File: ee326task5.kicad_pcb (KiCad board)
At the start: 2 copper layers, 41 parts, among them J1 694106106102, J2 Conn_01x03, J3 Conn_01x03, J4 Conn_01x03, J5 Conn_01x03, J6 2-1734592-4, SW1 MCU_RESET, SW2 PROVISIONING, SW3 WIFI_RESET, SW4 IO0, U1 ATSAM4S8BA-AU, U2 LDL1117S30R, U3 ESP32-WROOM-32, Y1 ABM7-12.000MHZ-D2Y-T

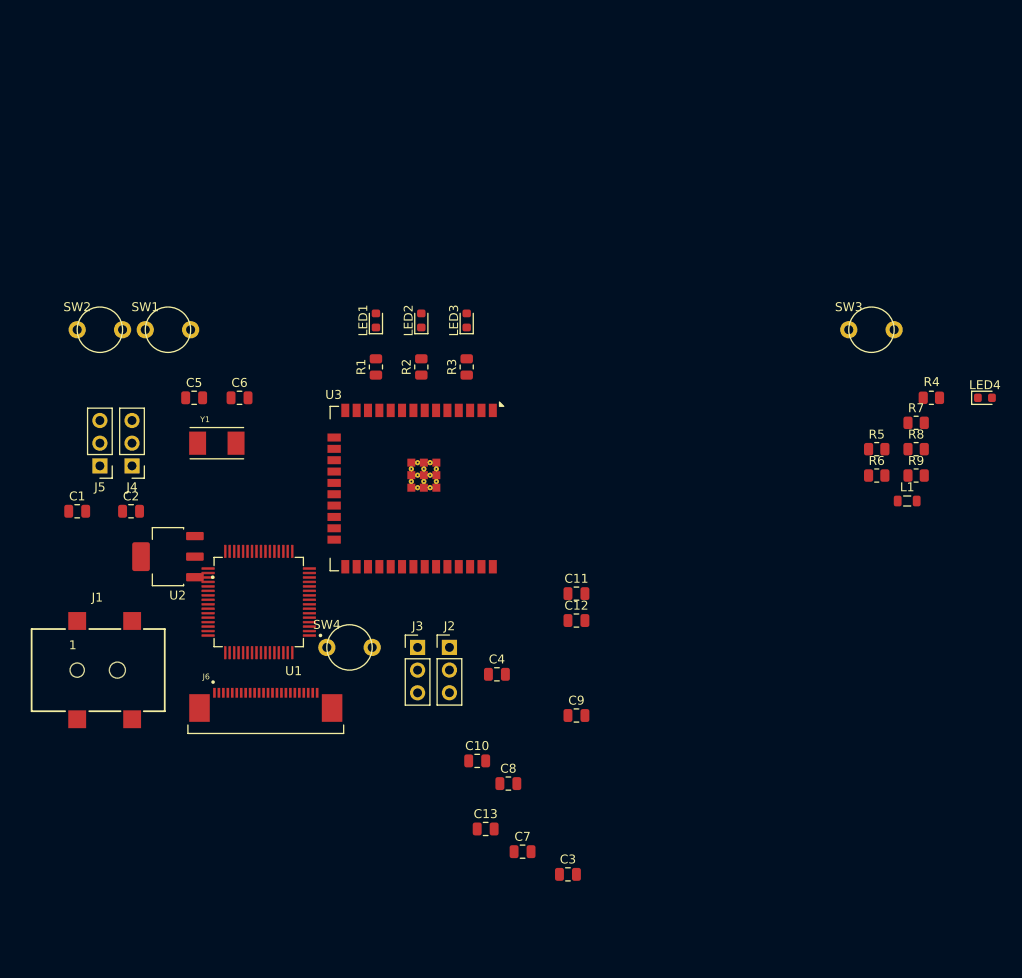
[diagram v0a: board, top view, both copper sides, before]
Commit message: fixed schematic errors
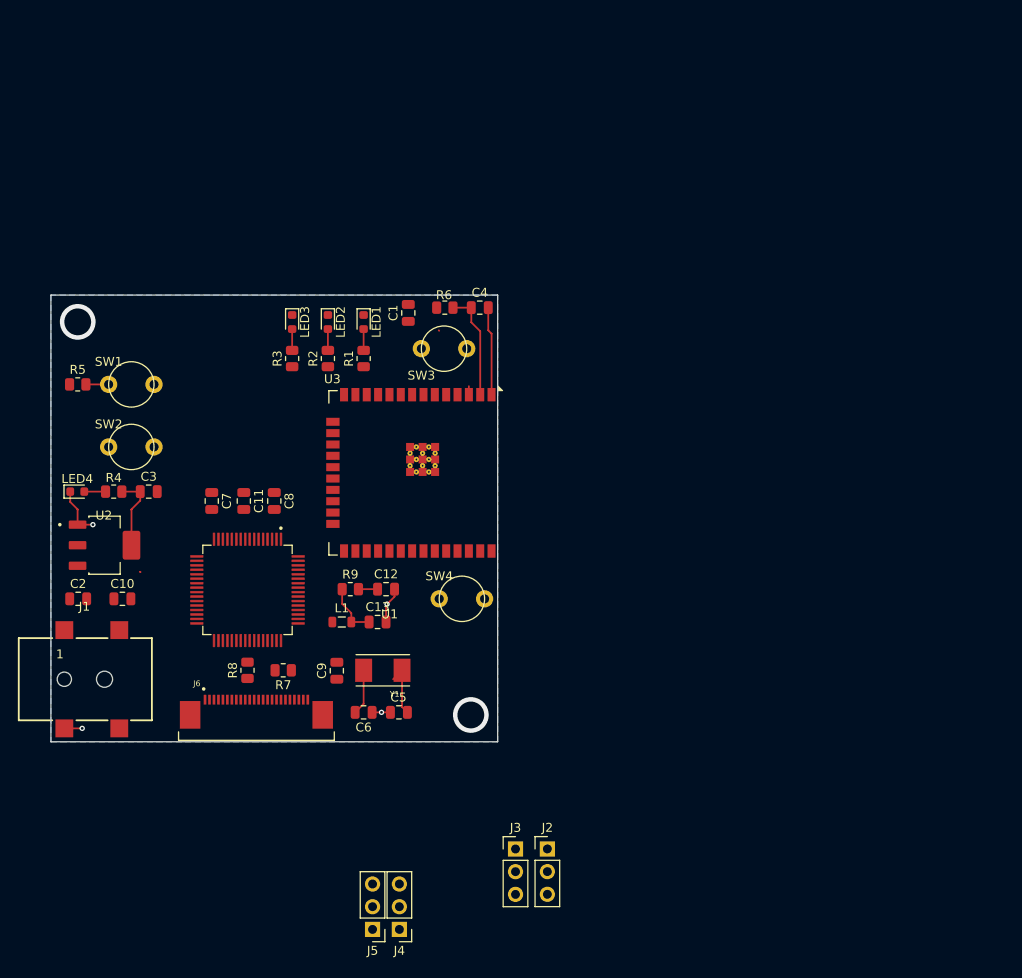
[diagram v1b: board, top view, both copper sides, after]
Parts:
- moved LED4 102.1 mm to (27.9, 74.0)
- moved R4 92.1 mm to (32.0, 74.0), turned to 180 degrees
- moved R5 89.7 mm to (28.0, 62.0)
- moved R8 78.8 mm to (47.0, 94.0), turned to 90 degrees
- moved R7 76.1 mm to (51.0, 94.0), turned to 180 degrees
- moved L1 64.7 mm to (57.6, 88.6)
- moved R9 64.6 mm to (58.5, 84.9)
- moved C3 63.5 mm to (35.9, 74.0)
- moved J5 60.2 mm to (61.0, 123.0)
- moved J4 59.9 mm to (64.0, 123.0)
- moved C7 52.4 mm to (43.0, 75.0), turned to -90 degrees
- moved R6 51.9 mm to (69.1, 53.4), turned to 180 degrees
- moved SW3 47.9 mm to (69.0, 58.0)
- moved C10 43.7 mm to (33.0, 86.0)
- moved C1 43.2 mm to (65.0, 54.0), turned to 90 degrees
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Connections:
- C11 pad 2: Net-(U1-VDDOUT) -> /VDD1V2
- U1 pad 8: Net-(U1-VDDOUT) -> /VDD1V2
- U2 pad 4: unconnected-(U2-VOUT__1-Pad4) -> /VDD3V0
- U3 pad 34: /DEBUG_TX -> /DEBUG_RX
- U3 pad 35: /DEBUG_RX -> /DEBUG_TX
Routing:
- net GND: track 0.00 -> 23.8 mm, vias 0 -> 4
- net /VDD3V0: track 0.00 -> 20.7 mm
- net Net-(C13-Pad1): track 0.00 -> 6.09 mm
- net /XTAL1: track 0.00 -> 5.59 mm
- net /XTAL2: track 0.00 -> 5.10 mm
- net /NRST: track 0.00 -> 2.55 mm
- net Net-(LED3-A): track 0.00 -> 2.39 mm
- net Net-(LED2-A): track 0.00 -> 2.39 mm
- net Net-(LED1-A): track 0.00 -> 2.39 mm
- net Net-(LED4-A): track 0.00 -> 2.38 mm
- net Net-(C12-Pad1): track 0.00 -> 2.14 mm
- net /EN: track 0.00 -> 1.02 mm
- net +5V: track 0.00 -> 0.85 mm
- net (no net): vias 0 -> 2
- added copper zone on B.Cu, net GND
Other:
- board outline added: 50 x 50 mm

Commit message: routing
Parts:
- added REF**: MountingHole_3mm, MountingHole:MountingHole_3mm, F.Cu at (33.0, 25.0)
- added REF**: MountingHole_3mm, MountingHole:MountingHole_3mm, F.Cu at (75.0, 67.0)
- moved J2 96.6 mm to (47.4, 23.3)
- moved J3 96.4 mm to (44.6, 23.3)
- moved J4 90.2 mm to (47.9, 34.2), turned to 0 degrees
- moved J5 89.4 mm to (50.6, 34.2), turned to 0 degrees
- moved PROVISION 35.0 mm to (34.0, 34.0), turned to 180 degrees
- moved LED4 32.0 mm to (42.0, 45.2), turned to -90 degrees
- moved R7 32.0 mm to (56.0, 62.4), turned to 0 degrees
- moved R8 31.8 mm to (50.0, 62.4), turned to 180 degrees
- moved C11 31.3 mm to (49.0, 43.8), turned to 180 degrees
- moved C12 31.3 mm to (66.5, 53.9)
- moved R9 31.3 mm to (62.5, 53.9)
- moved R1 31.3 mm to (64.0, 28.1)
- moved R2 31.3 mm to (60.0, 28.1)
- moved R3 31.3 mm to (56.0, 28.1)
- moved C10 31.3 mm to (37.0, 55.0)
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- renumbered LED3 to AP, SW4 to IO0, SW1 to MCU_RST, LED1 to Net, SW2 to PROVISION, SW3 to WIFI_RST, LED2 to WS
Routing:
- net /VDD3V0: track 20.7 -> 172.2 mm, vias 0 -> 21
- net GND: track 23.8 -> 104.8 mm, vias 4 -> 14
- net /EN: track 1.02 -> 50.3 mm, vias 0 -> 4
- net /NRST: track 2.55 -> 43.1 mm, vias 0 -> 1
- net /PB4: track 0.00 -> 39.1 mm, vias 0 -> 2
- net /SWO: track 0.00 -> 38.6 mm, vias 0 -> 4
- net /VDD1V2: track 0.00 -> 38.2 mm, vias 0 -> 2
- net /SWDCLK: track 0.00 -> 37.1 mm
- net /SWDIO: track 0.00 -> 35.7 mm
- net +5V: track 0.85 -> 36.2 mm, vias 0 -> 1
- net /PA2: track 0.00 -> 33.5 mm, vias 0 -> 2
- net /MCU_TX: track 0.00 -> 33.0 mm, vias 0 -> 2
- net /SCK: track 0.00 -> 32.2 mm, vias 0 -> 2
- net /MCU_RX: track 0.00 -> 30.4 mm, vias 0 -> 2
- net /DEBUG_TX: track 0.00 -> 30.1 mm, vias 0 -> 1
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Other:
- board text added: "3.0V"
- board text added: "5.0V"
- board text added: "DEBUG"
- board text added: "EE326 Webcam v1.0 February 17, 2026"
- board text added: "GND"
- board text added: "MCU"
- board text added: "NRST"
- board text added: "SWDCLK"
- board text added: "SWDIO"
- board text added: "SWO"

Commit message: finished
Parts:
- U3: footprint RF_Module:ESP32-WROOM-32E -> Library:ESP32-WROOM-32E
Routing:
- net GND: track 104.8 -> 137.0 mm, vias 14 -> 15
- net /VDD1V2: track 38.2 -> 56.9 mm
- net +5V: track 36.2 -> 42.4 mm
- net /VDD3V0: track 172.2 -> 173.7 mm, vias 21 -> 22
- net /SWO: track 38.6 -> 37.7 mm
- net /D7: track 13.7 -> 14.5 mm
